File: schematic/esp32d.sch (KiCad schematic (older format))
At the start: 47 parts, among them IC1 CP2102N-A01-GQFN28R, J1 Conn_02x08_Odd_Even, J2 Conn_02x08_Odd_Even, J4 Conn_01x02, Q1 SS8050-G, Q2 SS8050-G, SW1 SW_Push, U1 AMS1117-3.3, U2 ESP32-WROOM-32D, U3 DizzyBITLogo, U4 MCP73831-2-OT, U5 DizzyBIT-Layout

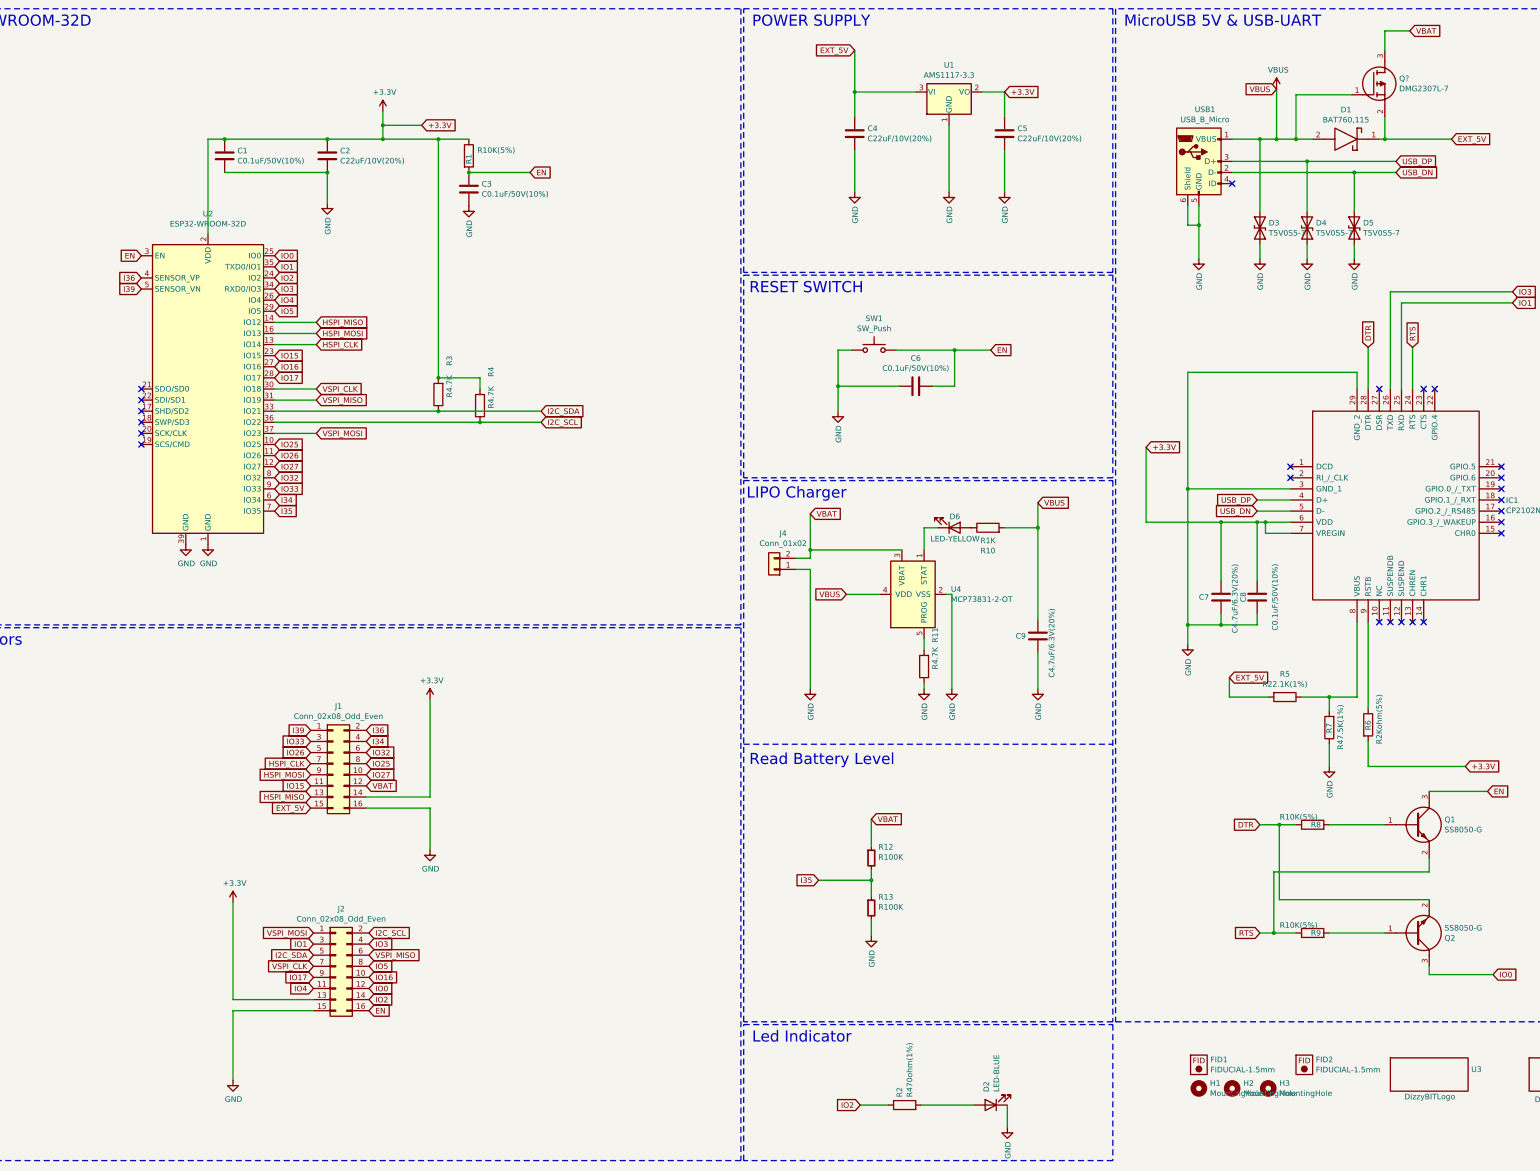
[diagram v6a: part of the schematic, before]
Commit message: Major Update. Changed pin configuration and board outline.
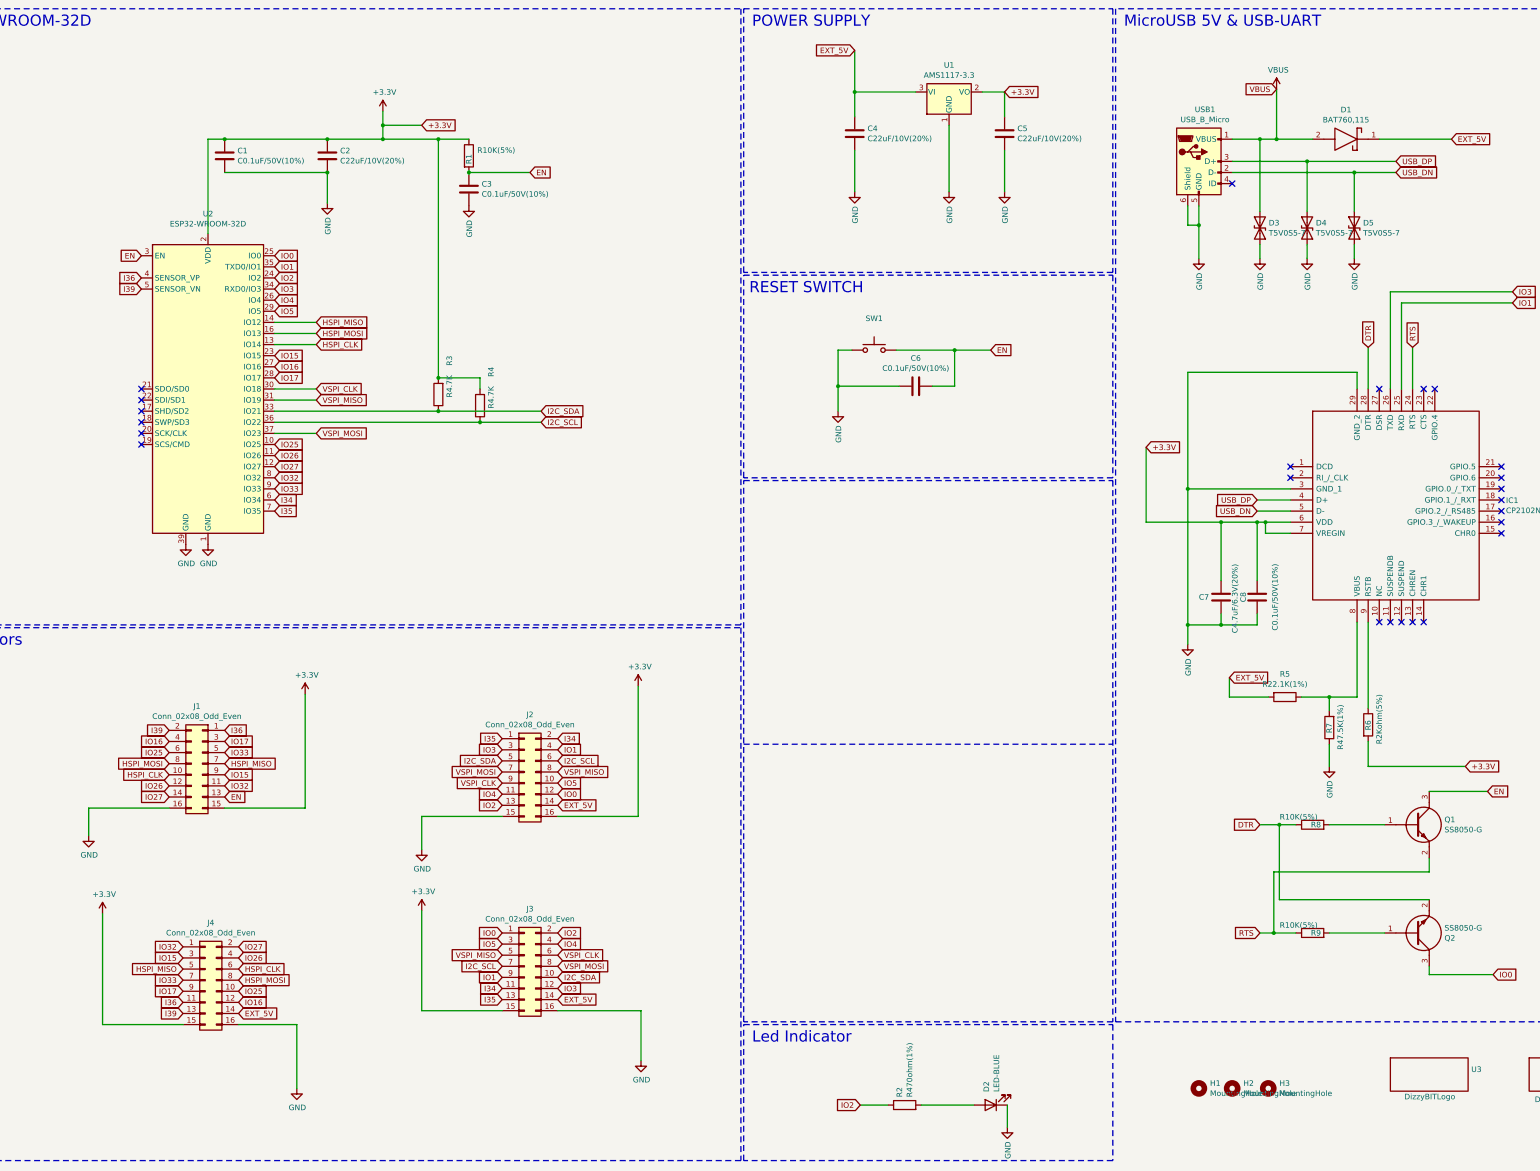
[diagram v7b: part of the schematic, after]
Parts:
- removed C9: C4.7uF/6.3V(20%), Capacitor_SMD:C_0603_1608Metric, symbol Device:C
- removed D6: LED-YELLOW, LED_SMD:LED_0805_2012Metric, symbol Device:LED
- removed FID1, FID2: FIDUCIAL-1.5mm, fab:FIDUCIAL-1.5mm, symbol pcb:FIDUCIAL-1.5mm
- removed J4: Conn_01x02, Connector_JST:JST_PH_S2B-PH-SM4-TB_1x02-1MP_P2.00mm_Horizontal, symbol Connector_Generic:Conn_01x02
- removed Q?: DMG2307L-7, SOT96P240X110-3N, symbol SamacSys_Parts:DMG2307L-7
- removed R10: R1K, Resistor_SMD:R_0805_2012Metric, symbol Device:R
- removed R11: R4.7K, Resistor_SMD:R_0603_1608Metric, symbol Device:R
- removed R12, R13: R100K, Resistor_SMD:R_0603_1608Metric, symbol _passive:R
- removed U4: MCP73831-2-OT, Package_TO_SOT_SMD:SOT-23-5, symbol Battery_Management:MCP73831-2-OT
- added J3, J4: Conn_02x08_Odd_Even, Connector_JST:JST_PUD_S16B-PUDSS-1_2x08_P2.00mm_Horizontal, symbol Connector_Generic:Conn_02x08_Odd_Even
- D2: dk_pn FC-A2012BK-470H2 -> LTST-C170TBKT
- J1, J2: footprint Connector_PinHeader_2.54mm:PinHeader_2x08_P2.54mm_Vertical -> Connector_PinSocket_2.54mm:PinSocket_2x08_P2.54mm_Vertical; pn PC104-003-2*8-B-1 -> PC104-013-2*8-B-1
- SW1: footprint Button_Switch_SMD:TL3340 -> Button_Switch_THT:SW_Tactile_SPST_Angled_PTS645Vx31-2LFS; dk_pn EG4627TR-ND -> (none); pn TL3340AF160QG -> PTS645VH39-2 LFS
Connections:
- net VBAT is gone; now on net IO26: J1.12 (Pin_12)
- net +3V3: now also J1.15 (Pin_15), J2.16 (Pin_16), J3.15 (Pin_15), J4.15 (Pin_15); no longer J1.14 (Pin_14), J2.13 (Pin_13)
- net EN: now also J1.13 (Pin_13); no longer J2.16 (Pin_16)
- net EXT_5V: now also J2.14 (Pin_14), J3.14 (Pin_14), J4.14 (Pin_14); no longer J1.15 (Pin_15)
- net GND: now also J3.16 (Pin_16), J4.16 (Pin_16)
- net HSPI_CLK: now also J1.10 (Pin_10), J4.6 (Pin_6); no longer J1.7 (Pin_7)
- net HSPI_MISO: now also J1.7 (Pin_7), J4.5 (Pin_5); no longer J1.13 (Pin_13)
- net HSPI_MOSI: now also J1.8 (Pin_8), J4.8 (Pin_8); no longer J1.9 (Pin_9)
- net I2C_SCL: now also J2.6 (Pin_6), J3.7 (Pin_7); no longer J2.2 (Pin_2)
- net I2C_SDA: now also J3.10 (Pin_10)
- net I34: now also J2.2 (Pin_2), J3.11 (Pin_11); no longer J1.4 (Pin_4)
- net I35: now also J2.1 (Pin_1), J3.13 (Pin_13)
- net I36: now also J1.1 (Pin_1), J4.11 (Pin_11); no longer J1.2 (Pin_2)
- net I39: now also J1.2 (Pin_2), J4.13 (Pin_13); no longer J1.1 (Pin_1)
- net IO0: now also J3.1 (Pin_1)
- net IO1: now also J2.4 (Pin_4), J3.9 (Pin_9); no longer J2.3 (Pin_3)
- net IO15: now also J1.9 (Pin_9), J4.3 (Pin_3); no longer J1.11 (Pin_11)
- net IO16: now also J1.4 (Pin_4), J4.12 (Pin_12); no longer J2.10 (Pin_10)
- net IO17: now also J1.3 (Pin_3), J4.9 (Pin_9); no longer J2.9 (Pin_9)
- net IO2: now also J2.13 (Pin_13), J3.2 (Pin_2); no longer J2.14 (Pin_14)
- net IO25: now also J1.6 (Pin_6), J4.10 (Pin_10); no longer J1.8 (Pin_8)
- net IO26: now also J4.4 (Pin_4); no longer J1.5 (Pin_5)
- net IO27: now also J1.14 (Pin_14), J4.2 (Pin_2); no longer J1.10 (Pin_10)
- net IO3: now also J2.3 (Pin_3), J3.12 (Pin_12); no longer J2.4 (Pin_4)
- net IO32: now also J1.11 (Pin_11), J4.1 (Pin_1); no longer J1.6 (Pin_6)
- net IO33: now also J1.5 (Pin_5), J4.7 (Pin_7); no longer J1.3 (Pin_3)
- net IO4: now also J3.4 (Pin_4)
- net IO5: now also J2.10 (Pin_10), J3.3 (Pin_3); no longer J2.8 (Pin_8)
- net VSPI_CLK: now also J2.9 (Pin_9), J3.6 (Pin_6); no longer J2.7 (Pin_7)
- net VSPI_MISO: now also J2.8 (Pin_8), J3.5 (Pin_5); no longer J2.6 (Pin_6)
- net VSPI_MOSI: now also J2.7 (Pin_7), J3.8 (Pin_8); no longer J2.1 (Pin_1)
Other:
- note removed: "LIPO Charger"
- note removed: "Read Battery Level"
- moved on the sheet: J1, J2
